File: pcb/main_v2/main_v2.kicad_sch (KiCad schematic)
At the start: 1 part, among them J102 Conn_02x06_Odd_Even

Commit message: updated schematic after review
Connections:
- net CONN-1 renamed power/Power Enable
- net CONN-2 renamed power/Power Faulty
- net CONN-3 renamed transmitter/PA Enable
- net CONN-4 renamed transmitter/PA DET Output
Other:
- sheet oscillator ports: added Oscillator Rx, Oscillator Tx; removed none
- sheet power ports: added Power Enable, Power Faulty; removed none
- sheet receiver ports: added Oscillator Rx; removed none
- sheet transmitter ports: added Oscillator Tx, PA DET Output, PA Enable; removed none
- moved on the sheet: J102

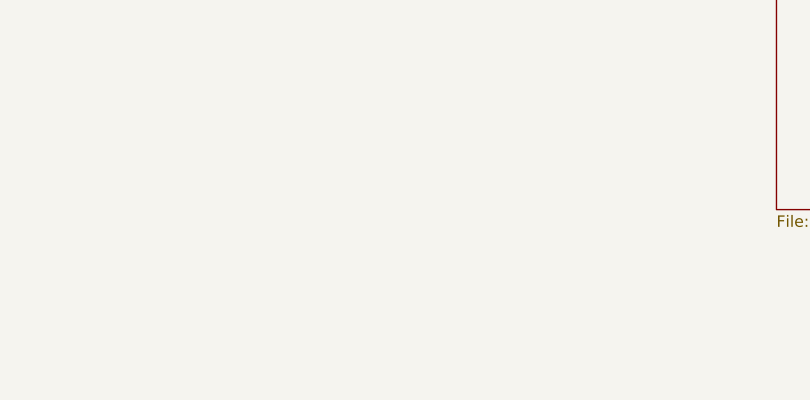
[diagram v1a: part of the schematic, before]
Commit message: added new osci
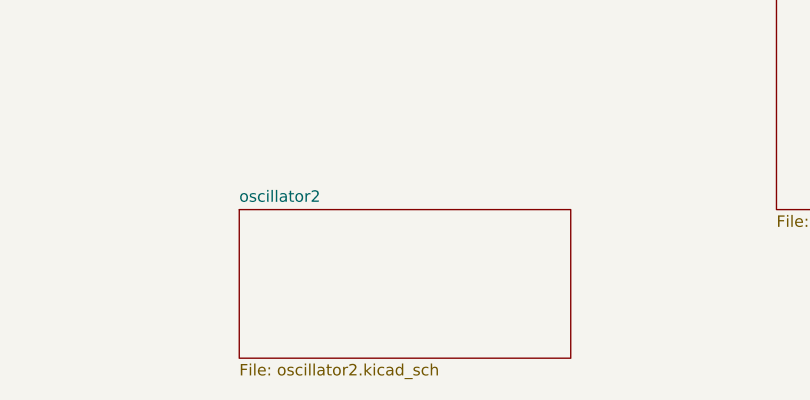
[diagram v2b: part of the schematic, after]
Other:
- added sheet oscillator2 (oscillator2.kicad_sch)
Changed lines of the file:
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@@
+	)
+	(sheet
+		(at 125.73 142.24)
+		(size 36.83 16.51)
+		(exclude_from_sim no)
+		(in_bom yes)
+		(on_board yes)
+		(dnp no)
+		(fields_autoplaced yes)
+		(stroke
+			(width 0.1524)
+			(type solid)
+		)
+		(fill
+			(color 0 0 0 0)
+		)
+		(property "Sheetname" "oscillator2"
+			(at 125.73 141.5284 0)
+			(show_name no)
+			(do_not_autoplace no)
+			(effects
+				(font
+					(size 1.27 1.27)
+				)
+				(justify left bottom)
+			)
+		)
+		(property "Sheetfile" "oscillator2.kicad_sch"
+			(at 125.73 159.3346 0)
+			(show_name no)
+			(do_not_autoplace no)
+			(effects
+				(font
+					(size 1.27 1.27)
+				)
+				(justify left top)
+			)
+		)
+		(instances
+			(project "main_v2"
+				(path "/0599865e-4bed-44f1-b46e-4b55335b49b2"
+					(page "6")
+				)
+			)
+		)
 	)
 	(sheet

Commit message: updated schematic
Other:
- added sheet IO Interface (io.kicad_sch)
- sheet oscillator2 ports: added Oscillator Rx, Oscillator Tx, PLL: Chip Enable, PLL: Lock Detect, PLL: MUXOUT, PLL: Power Down, SPI: CLK, SPI: DATA, SPI: Load Enable; removed none
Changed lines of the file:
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@@
+	)
+	(sheet
+		(at 124.46 170.18)
+		(size 39.37 16.51)
+		(exclude_from_sim no)
+		(in_bom yes)
+		(on_board yes)
+		(dnp no)
+		(fields_autoplaced yes)
+		(stroke
+			(width 0.1524)
+			(type solid)
+		)
+		(fill
+			(color 0 0 0 0)
+		)
+		(property "Sheetname" "IO Interface"
+			(at 124.46 169.4684 0)
+			(show_name no)
+			(do_not_autoplace no)
+			(effects
+				(font
+					(size 1.27 1.27)
+				)
+				(justify left bottom)
+			)
+		)
+		(property "Sheetfile" "io.kicad_sch"
+			(at 124.46 187.2746 0)
+			(show_name no)
+			(do_not_autoplace no)
+			(effects
+				(font
+					(size 1.27 1.27)
+				)
+				(justify left top)
+			)
+		)
+		(instances
+			(project "main_v2"
+				(path "/0599865e-4bed-44f1-b46e-4b55335b49b2"
+					(page "7")
+				)
+			)
+		)
 	)
 	(sheet
@@
 			)
 		)
+		(pin "Oscillator Rx" input
+			(at 144.78 142.24 90)
+			(effects
+				(font
+					(size 1.27 1.27)
+				)
+				(justify right)
+			)
+		)
+		(pin "Oscillator Tx" input
+			(at 140.97 142.24 90)
+			(effects
+				(font
+					(size 1.27 1.27)
+				)
+				(justify right)
+			)
+		)
+		(pin "PLL: Chip Enable" input
+			(at 125.73 156.21 180)
+			(effects
+				(font
+					(size 1.27 1.27)
+				)
+				(justify left)
+			)
+		)
+		(pin "PLL: Lock Detect" input
+			(at 125.73 151.13 180)
+			(effects
+				(font
+					(size 1.27 1.27)
+				)
+				(justify left)
+			)
+		)
+		(pin "PLL: MUXOUT" input
+			(at 125.73 148.59 180)
+			(effects
+				(font
+					(size 1.27 1.27)
+				)
+				(justify left)
+			)
+		)
+		(pin "PLL: Power Down" input
+			(at 125.73 146.05 180)
+			(effects
+				(font
+					(size 1.27 1.27)
+				)
+				(justify left)
+			)
+		)
+		(pin "SPI: CLK" input
+			(at 162.56 144.78 0)
+			(effects
+				(font
+					(size 1.27 1.27)
+				)
+				(justify right)
+			)
+		)
+		(pin "SPI: DATA" input
+			(at 162.56 147.32 0)
+			(effects
+				(font
+					(size 1.27 1.27)
+				)
+				(justify right)
+			)
+		)
+		(pin "SPI: Load Enable" input
+			(at 162.56 149.86 0)
+			(effects
+				(font
+					(size 1.27 1.27)
+				)
+				(justify right)
+			)
+		)

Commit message: updarted schematic and simulation
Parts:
- removed J102: Conn_02x06_Odd_Even, symbol Connector_Generic:Conn_02x06_Odd_Even
- added H101, H102, H103, H104: MountingHole, MountingHole:MountingHole_2.2mm_M2, symbol Mechanical:MountingHole
- added J101, J102, J103, J104: Conn_Coaxial, Connector_Coaxial:SMA_Amphenol_132289_EdgeMount, symbol Connector:Conn_Coaxial
- added J105: Barrel_Jack, Connector_BarrelJack:BarrelJack_CUI_PJ-063AH_Horizontal_CircularHoles, symbol Connector:Barrel_Jack
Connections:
- net GND: now also J101.2 (Ext), J102.2 (Ext), J103.2 (Ext), J104.2 (Ext)
- new net power/DC GND: J105.2
- new net power/DC Power: J105.1
- new net receiver/Rx In: J101.1 (In)
- new net receiver/Rx Out: J102.1 (In)
- new net transmitter/Tx In: J103.1 (In)
- new net transmitter/Tx Out: J104.1 (In)
- no-connect marks 2 -> 0
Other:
- sheet oscillator2 renamed Phase locked loop
- removed sheet oscillator
- added sheet Oscillator Splitter (splitter.kicad_sch)
- sheet IO Interface ports: added PA DET Output, PA Enable, PLL: Chip Enable, PLL: Lock Detect, PLL: MUXOUT, PLL: Power Down, Power Enable, Power Faulty, SPI: CLK, SPI: DATA, SPI: Load Enable; removed none
- sheet Phase locked loop: file oscillator2.kicad_sch -> pll.kicad_sch
- sheet Phase locked loop ports: added Oscillator +, Oscillator -; removed Oscillator Rx, Oscillator Tx
- sheet power ports: added DC GND, DC Power; removed none
- sheet receiver ports: added Rx In, Rx Out; removed none
- sheet transmitter ports: added Tx In, Tx Out; removed none
- note added: "RFSOC: https://www.realdigital.org/downloads/15456c97a4fe5a1ee66208c5aa3894bb.pdf ADC: max input power: 14.6 dBm attenuation range: 27 dB input bandwith: 6 GHz DAC: Max output power: -18.5 to 6.5 dBm current max: 40.5 mA"
- note removed: "GPIO IN: Enable Power Managemnet"
- note removed: "GPIO IN: Enable Tx Amplifier"
- note removed: "GPIO Out: Fault Signal"
- note removed: "GPIO Out: Tx Amplifier Power Detector"

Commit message: updated io schematic
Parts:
- renumbered H103 to H101, H104 to H102, H101 to H103, H102 to H104, J102 to J101, J104 to J102, J101 to J103, J103 to J104
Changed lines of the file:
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@@
 		(dnp no)
 		(fields_autoplaced yes)
-		(property "Reference" "H101"
+		(property "Reference" "H103"
 			(at 25.4 31.7499 0)
 			(show_name no)
@@
 			(project "main_v2"
 				(path "/0599865e-4bed-44f1-b46e-4b55335b49b2"
-					(reference "H101")
+					(reference "H103")
 					(unit 1)
 				)
@@
 		(in_pos_files yes)
 		(dnp no)
-		(property "Reference" "J101"
+		(property "Reference" "J103"
 			(at 78.74 42.2031 0)
 			(show_name no)
@@
 			(project "main_v2"
 				(path "/0599865e-4bed-44f1-b46e-4b55335b49b2"
-					(reference "J101")
+					(reference "J103")
 					(unit 1)
 				)
@@
 		(dnp no)
 		(fields_autoplaced yes)
-		(property "Reference" "H102"
+		(property "Reference" "H104"
 			(at 44.45 31.7499 0)
 			(show_name no)
@@
 			(project "main_v2"
 				(path "/0599865e-4bed-44f1-b46e-4b55335b49b2"
-					(reference "H102")
+					(reference "H104")
 					(unit 1)
 				)
@@
 		(in_pos_files yes)
 		(dnp no)
-		(property "Reference" "J102"
+		(property "Reference" "J101"
 			(at 162.56 33.3131 0)
 			(show_name no)
@@
 			(project "main_v2"
 				(path "/0599865e-4bed-44f1-b46e-4b55335b49b2"
-					(reference "J102")
+					(reference "J101")
 					(unit 1)
 				)
@@
 		(dnp no)
 		(fields_autoplaced yes)
-		(property "Reference" "#PWR0103"
+		(property "Reference" "#PWR0104"
 			(at 182.88 57.15 0)
 			(hide yes)
@@
 			(project "main_v2"
 				(path "/0599865e-4bed-44f1-b46e-4b55335b49b2"
-					(reference "#PWR0103")
+					(reference "#PWR0104")
 					(unit 1)
 				)
@@
 		(dnp no)
 		(fields_autoplaced yes)
-		(property "Reference" "#PWR0104"
+		(property "Reference" "#PWR0102"
 			(at 259.08 45.72 0)
 			(hide yes)
@@
 			(project "main_v2"
 				(path "/0599865e-4bed-44f1-b46e-4b55335b49b2"
-					(reference "#PWR0104")
+					(reference "#PWR0102")
 					(unit 1)
 				)
@@
 		(in_pos_files yes)
 		(dnp no)
-		(property "Reference" "J103"
+		(property "Reference" "J104"
 			(at 179.07 44.7431 0)
 			(show_name no)
@@
 			(project "main_v2"
 				(path "/0599865e-4bed-44f1-b46e-4b55335b49b2"
-					(reference "J103")
+					(reference "J104")
 					(unit 1)
 				)
@@
 		(in_pos_files yes)
 		(dnp no)
-		(property "Reference" "J104"
+		(property "Reference" "J102"
 			(at 262.89 33.3131 0)
 			(show_name no)
@@
 			(project "main_v2"
 				(path "/0599865e-4bed-44f1-b46e-4b55335b49b2"
-					(reference "J104")
+					(reference "J102")
 					(unit 1)
 				)
@@
 		(dnp no)
 		(fields_autoplaced yes)
-		(property "Reference" "#PWR0102"
+		(property "Reference" "#PWR0101"
 			(at 158.75 45.72 0)
 			(hide yes)
@@
 			(project "main_v2"
 				(path "/0599865e-4bed-44f1-b46e-4b55335b49b2"
-					(reference "#PWR0102")
+					(reference "#PWR0101")
 					(unit 1)
 				)
@@
 		(dnp no)
 		(fields_autoplaced yes)
-		(property "Reference" "#PWR0101"
+		(property "Reference" "#PWR0103"
 			(at 82.55 54.61 0)
 			(hide yes)
@@
 			(project "main_v2"
 				(path "/0599865e-4bed-44f1-b46e-4b55335b49b2"
-					(reference "#PWR0101")
+					(reference "#PWR0103")
 					(unit 1)
 				)
@@
 		(dnp no)
 		(fields_autoplaced yes)
-		(property "Reference" "H103"
+		(property "Reference" "H101"
 			(at 25.4 24.1299 0)
 			(show_name no)
@@
 			(project "main_v2"
 				(path "/0599865e-4bed-44f1-b46e-4b55335b49b2"
-					(reference "H103")
+					(reference "H101")
 					(unit 1)
 				)
@@
 		(dnp no)
 		(fields_autoplaced yes)
-		(property "Reference" "H104"
+		(property "Reference" "H102"
 			(at 44.45 24.1299 0)
 			(show_name no)
@@
 			(project "main_v2"
 				(path "/0599865e-4bed-44f1-b46e-4b55335b49b2"
-					(reference "H104")
-					(unit 1)
-				)
+					(reference "H102")
+					(unit 1)
+				)

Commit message: update bom
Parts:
- removed J105: Barrel_Jack, Connector_BarrelJack:BarrelJack_CUI_PJ-063AH_Horizontal_CircularHoles, symbol Connector:Barrel_Jack
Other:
- sheet IO Interface ports: added PLL: Lock Detect Out, Power Faulty Out; removed PLL: Lock Detect, Power Faulty
- sheet power ports: added none; removed DC GND, DC Power

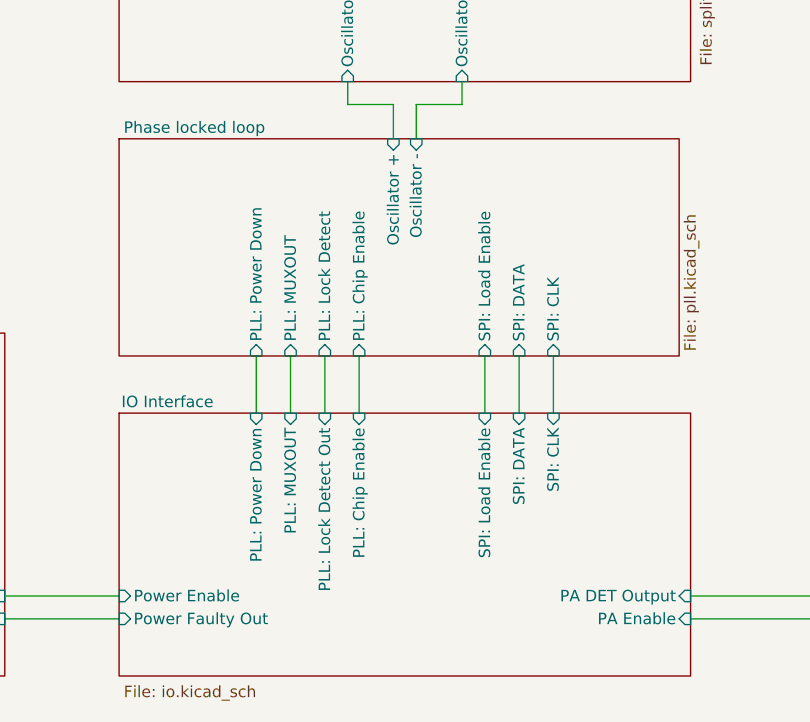
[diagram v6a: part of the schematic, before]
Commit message: updated spi connection
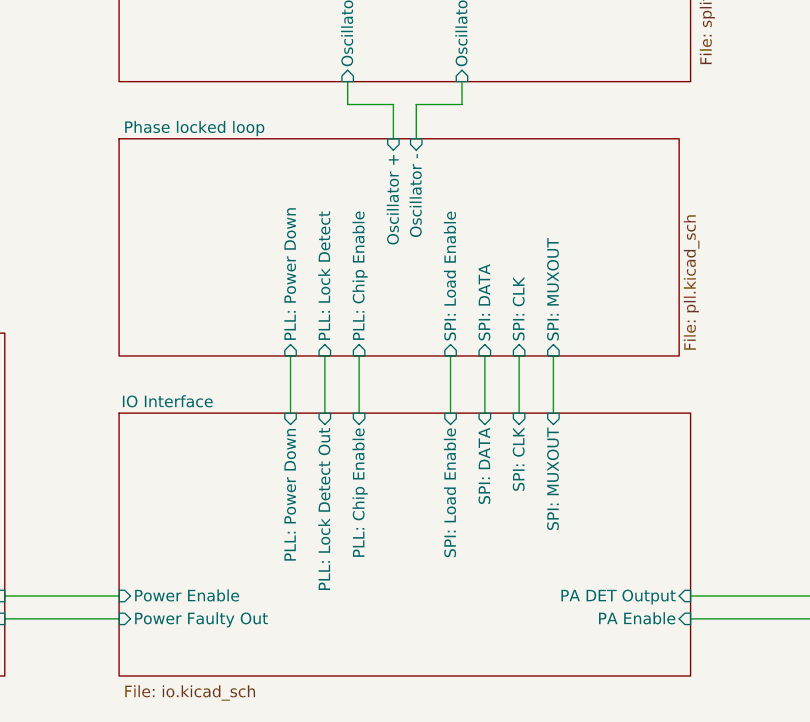
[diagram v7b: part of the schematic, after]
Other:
- sheet IO Interface ports: added SPI: MUXOUT; removed PLL: MUXOUT
- sheet Phase locked loop ports: added SPI: MUXOUT; removed PLL: MUXOUT
